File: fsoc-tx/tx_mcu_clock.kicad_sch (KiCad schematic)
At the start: 30 parts, among them J3 FTSH-105-01-L-DV-K, SW1 SW_RESET, SW2 USB_BOOT, U3 RP2354A, Y1 ABM8-272-T3, Y2 ASTX-H11-10.000MHz-T

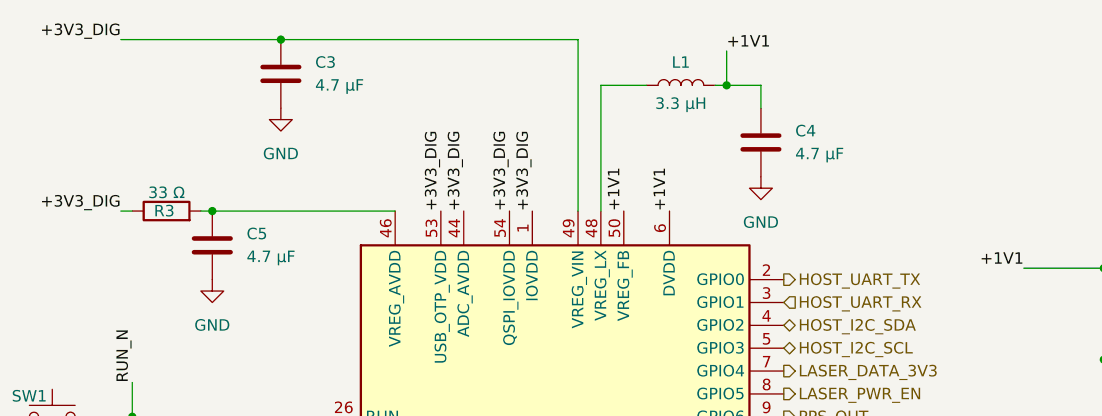
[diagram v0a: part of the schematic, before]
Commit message: ERC error excluded: TPS22919 QOD tied to VOUT intentionally
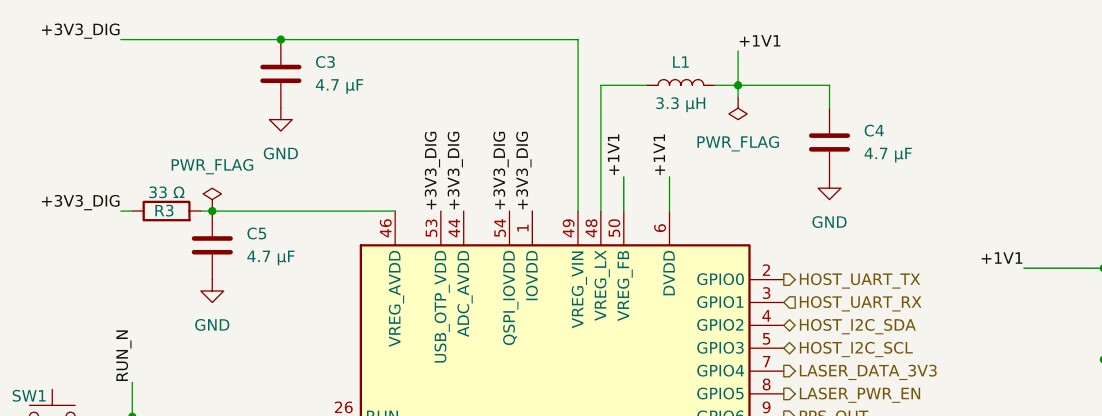
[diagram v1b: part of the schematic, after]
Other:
- moved on the sheet: C4
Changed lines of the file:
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@@
 	)
 	(junction
-		(at 179.07 29.21)
-		(diameter 0)
-		(color 0 0 0 0)
-	)
-	(junction
 		(at 199.39 148.59)
 		(diameter 0)
@@
 	)
 	(junction
+		(at 180.34 29.21)
+		(diameter 0)
+		(color 0 0 0 0)
+	)
+	(junction
 		(at 222.25 100.33)
 		(diameter 0)
@@
 	(wire
 		(pts
-			(xy 182.88 29.21) (xy 179.07 29.21)
+			(xy 190.5 29.21) (xy 180.34 29.21)
 		)
 		(stroke
@@
 	(wire
 		(pts
+			(xy 180.34 30.48) (xy 180.34 29.21)
+		)
+		(stroke
+			(width 0)
+			(type default)
+		)
+	)
+	(wire
+		(pts
 			(xy 111.76 148.59) (xy 118.11 148.59)
 		)
@@
 	(wire
 		(pts
-			(xy 179.07 25.4) (xy 179.07 29.21)
+			(xy 180.34 25.4) (xy 180.34 29.21)
 		)
 		(stroke
@@
 	(wire
 		(pts
-			(xy 177.8 29.21) (xy 179.07 29.21)
+			(xy 177.8 29.21) (xy 180.34 29.21)
 		)
 		(stroke
@@
 	(wire
 		(pts
+			(xy 167.64 39.37) (xy 167.64 43.18)
+		)
+		(stroke
+			(width 0)
+			(type default)
+		)
+	)
+	(wire
+		(pts
 			(xy 111.76 83.82) (xy 116.84 83.82)
 		)
@@
 	(wire
 		(pts
-			(xy 182.88 31.75) (xy 182.88 29.21)
+			(xy 190.5 31.75) (xy 190.5 29.21)
 		)
 		(stroke
@@
 	(wire
 		(pts
+			(xy 172.72 39.37) (xy 172.72 43.18)
+		)
+		(stroke
+			(width 0)
+			(type default)
+		)
+	)
+	(wire
+		(pts
 			(xy 130.81 77.47) (xy 130.81 76.2)
 		)
@@
 	)
 	(label "+1V1"
-		(at 167.64 43.18 90)
+		(at 167.64 39.37 90)
 		(effects
 			(font
@@
 	)
 	(label "+1V1"
-		(at 172.72 43.18 90)
+		(at 172.72 39.37 90)
 		(effects
 			(font
@@
 	)
 	(label "+1V1"
-		(at 179.07 25.4 0)
+		(at 180.34 25.4 0)
 		(effects
 			(font
@@
 	)
 	(symbol
+		(lib_id "power:PWR_FLAG")
+		(at 121.92 43.18 0)
+		(unit 1)
+		(body_style 1)
+		(exclude_from_sim no)
+		(in_bom yes)
+		(on_board yes)
+		(in_pos_files yes)
+		(dnp no)
+		(fields_autoplaced yes)
+		(property "Reference" "#FLG04"
+			(at 121.92 41.275 0)
+			(hide yes)
+			(show_name no)
+			(do_not_autoplace no)
+			(effects
+				(font
+					(size 1.27 1.27)
+				)
+			)
+		)
+		(property "Value" "PWR_FLAG"
+			(at 121.92 38.1 0)
+			(show_name no)
+			(do_not_autoplace no)
+			(effects
+				(font
+					(size 1.27 1.27)
+				)
+			)
+		)
+		(property "Footprint" ""
+			(at 121.92 43.18 0)
+			(hide yes)
+			(show_name no)
+			(do_not_autoplace no)
+			(effects
+				(font
+					(size 1.27 1.27)
+				)
+			)
+		)
+		(property "Datasheet" ""
+			(at 121.92 43.18 0)
+			(hide yes)
+			(show_name no)
+			(do_not_autoplace no)
+			(effects
+				(font
+					(size 1.27 1.27)
+				)
+			)
+		)
+		(property "Description" "Special symbol for telling ERC where power comes from"
+			(at 121.92 43.18 0)
+			(hide yes)
+			(show_name no)
+			(do_not_autoplace no)
+			(effects
+				(font
+					(size 1.27 1.27)
+				)
+			)
+		)
+		(pin "1"
+		)
+		(instances
+			(project "fsoc-tx"
+				(path "/d92cb11a-a3ee-43a3-bd30-881774176ced/1d4fb2f8-c912-4583-8b21-2ebadb633d8f"
+					(reference "#FLG04")
+					(unit 1)
+				)
+			)
+		)
+	)
+	(symbol
 		(lib_id "Switch:SW_Push")
 		(at 106.68 83.82 0)
@@
 	)
 	(symbol
+		(lib_id "power:PWR_FLAG")
+		(at 180.34 30.48 180)
+		(unit 1)
+		(body_style 1)
+		(exclude_from_sim no)
+		(in_bom yes)
+		(on_board yes)
+		(in_pos_files yes)
+		(dnp no)
+		(fields_autoplaced yes)
+		(property "Reference" "#FLG03"
+			(at 180.34 32.385 0)
+			(hide yes)
+			(show_name no)
+			(do_not_autoplace no)
+			(effects
+				(font
+					(size 1.27 1.27)
+				)
+			)
+		)
+		(property "Value" "PWR_FLAG"
+			(at 180.34 35.56 0)
+			(show_name no)
+			(do_not_autoplace no)
+			(effects
+				(font
+					(size 1.27 1.27)
+				)
+			)
+		)
+		(property "Footprint" ""
+			(at 180.34 30.48 0)
+			(hide yes)
+			(show_name no)
+			(do_not_autoplace no)
+			(effects
+				(font
+					(size 1.27 1.27)
+				)
+			)
+		)
+		(property "Datasheet" ""
+			(at 180.34 30.48 0)
+			(hide yes)
+			(show_name no)
+			(do_not_autoplace no)
+			(effects
+				(font
+					(size 1.27 1.27)
+				)
+			)
+		)
+		(property "Description" "Special symbol for telling ERC where power comes from"
+			(at 180.34 30.48 0)
+			(hide yes)
+			(show_name no)
+			(do_not_autoplace no)
+			(effects
+				(font
+					(size 1.27 1.27)
+				)
+			)
+		)
+		(pin "1"
+		)
+		(instances
+			(project "fsoc-tx"
+				(path "/d92cb11a-a3ee-43a3-bd30-881774176ced/1d4fb2f8-c912-4583-8b21-2ebadb633d8f"
+					(reference "#FLG03")
+					(unit 1)
+				)
+			)
+		)
+	)
+	(symbol
 		(lib_id "Device:R")
 		(at 116.84 43.18 90)
@@
 	(symbol
 		(lib_id "Device:C")
-		(at 182.88 35.56 0)
+		(at 190.5 35.56 0)
 		(unit 1)
 		(body_style 1)
@@
 		(fields_autoplaced yes)
 		(property "Reference" "C4"
-			(at 186.69 34.2899 0)
+			(at 194.31 34.2899 0)
 			(show_name no)
 			(do_not_autoplace no)
@@
 		)
 		(property "Value" "4.7 µF"
-			(at 186.69 36.8299 0)
+			(at 194.31 36.8299 0)
 			(show_name no)
 			(do_not_autoplace no)
@@
 		)
 		(property "Footprint" ""
-			(at 183.8452 39.37 0)
+			(at 191.4652 39.37 0)
 			(hide yes)
 			(show_name no)
@@
 		)
 		(property "Datasheet" ""
-			(at 182.88 35.56 0)
+			(at 190.5 35.56 0)
 			(hide yes)
 			(show_name no)
@@
 		)
 		(property "Description" "Unpolarized capacitor"
-			(at 182.88 35.56 0)
+			(at 190.5 35.56 0)
 			(hide yes)
 			(show_name no)
@@
 	(symbol
 		(lib_id "power:GND")
-		(at 182.88 39.37 0)
+		(at 190.5 39.37 0)
 		(unit 1)
 		(body_style 1)
@@
 		(fields_autoplaced yes)
 		(property "Reference" "#PWR011"
-			(at 182.88 45.72 0)
+			(at 190.5 45.72 0)
 			(hide yes)
 			(show_name no)
@@
 		)
 		(property "Value" "GND"
-			(at 182.88 44.45 0)
+			(at 190.5 44.45 0)
 			(show_name no)
 			(do_not_autoplace no)
@@
 		)
 		(property "Footprint" ""
-			(at 182.88 39.37 0)
+			(at 190.5 39.37 0)
 			(hide yes)
 			(show_name no)
@@
 		)
 		(property "Datasheet" ""
-			(at 182.88 39.37 0)
+			(at 190.5 39.37 0)
 			(hide yes)
 			(show_name no)
@@
 		)
 		(property "Description" "Power symbol creates a global label with name \"GND\" , ground"
-			(at 182.88 39.37 0)
+			(at 190.5 39.37 0)
 			(hide yes)
 			(show_name no)

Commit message: TX: fixing unassigned footprints
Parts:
- C10, C11, C12, C13, C14, C15, C16, C17, C18, C19, C20, C6, C8, C9: footprint (none) -> Capacitor_SMD:C_0603_1608Metric
- C3, C4, C5, C7: footprint (none) -> Capacitor_SMD:C_0805_2012Metric
- L1: footprint (none) -> fsoc_footprints:AOTA-B201610S3R3-101-T
- R3, R4, R5, R6, R7: footprint (none) -> Resistor_SMD:R_0603_1608Metric
- SW1, SW2: footprint (none) -> Button_Switch_SMD:SW_SPST_PTS645Sx43SMTR92
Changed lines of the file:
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@@
 			)
 		)
-		(property "Footprint" ""
+		(property "Footprint" "Capacitor_SMD:C_0603_1608Metric"
 			(at 162.8648 148.59 0)
 			(hide yes)
@@
 			)
 		)
-		(property "Footprint" ""
+		(property "Footprint" "Capacitor_SMD:C_0603_1608Metric"
 			(at 220.98 70.8152 0)
 			(hide yes)
@@
 			)
 		)
-		(property "Footprint" ""
+		(property "Footprint" "fsoc_footprints:AOTA-B201610S3R3-101-T"
 			(at 173.99 29.21 0)
 			(hide yes)
@@
 			)
 		)
-		(property "Footprint" ""
+		(property "Footprint" "Capacitor_SMD:C_0603_1608Metric"
 			(at 151.4348 148.59 0)
 			(hide yes)
@@
 			)
 		)
-		(property "Footprint" ""
+		(property "Footprint" "Capacitor_SMD:C_0603_1608Metric"
 			(at 175.5648 148.59 0)
 			(hide yes)
@@
 			)
 		)
-		(property "Footprint" ""
+		(property "Footprint" "Capacitor_SMD:C_0603_1608Metric"
 			(at 223.2152 109.22 0)
 			(hide yes)
@@
 			)
 		)
-		(property "Footprint" ""
+		(property "Footprint" "Capacitor_SMD:C_0603_1608Metric"
 			(at 113.9952 121.92 0)
 			(hide yes)
@@
 			)
 		)
-		(property "Footprint" ""
+		(property "Footprint" "Capacitor_SMD:C_0603_1608Metric"
 			(at 113.9952 104.14 0)
 			(hide yes)
@@
 			)
 		)
-		(property "Footprint" ""
+		(property "Footprint" "Capacitor_SMD:C_0805_2012Metric"
 			(at 228.6 58.7248 0)
 			(hide yes)
@@
 			)
 		)
-		(property "Footprint" ""
+		(property "Footprint" "Capacitor_SMD:C_0603_1608Metric"
 			(at 209.8548 148.59 0)
 			(hide yes)
@@
 			)
 		)
-		(property "Footprint" ""
+		(property "Footprint" "Capacitor_SMD:C_0603_1608Metric"
 			(at 117.1448 148.59 0)
 			(hide yes)
@@
 			)
 		)
-		(property "Footprint" ""
+		(property "Footprint" "Capacitor_SMD:C_0603_1608Metric"
 			(at 186.9948 148.59 0)
 			(hide yes)
@@
 			)
 		)
-		(property "Footprint" ""
+		(property "Footprint" "Capacitor_SMD:C_0805_2012Metric"
 			(at 122.8852 50.8 0)
 			(hide yes)
@@
 			)
 		)
-		(property "Footprint" ""
+		(property "Footprint" "Capacitor_SMD:C_0603_1608Metric"
 			(at 128.5748 148.59 0)
 			(hide yes)
@@
 			)
 		)
-		(property "Footprint" ""
+		(property "Footprint" "Button_Switch_SMD:SW_SPST_PTS645Sx43SMTR92"
 			(at 106.68 78.74 0)
 			(hide yes)
@@
 			)
 		)
-		(property "Footprint" ""
+		(property "Footprint" "Resistor_SMD:R_0603_1608Metric"
 			(at 116.84 44.958 90)
 			(hide yes)
@@
 			)
 		)
-		(property "Footprint" ""
+		(property "Footprint" "Capacitor_SMD:C_0603_1608Metric"
 			(at 198.4248 148.59 0)
 			(hide yes)
@@
 			)
 		)
-		(property "Footprint" ""
+		(property "Footprint" "Resistor_SMD:R_0603_1608Metric"
 			(at 120.65 85.598 90)
 			(hide yes)
@@
 			)
 		)
-		(property "Footprint" ""
+		(property "Footprint" "Resistor_SMD:R_0603_1608Metric"
 			(at 128.27 112.522 90)
 			(hide yes)
@@
 			)
 		)
-		(property "Footprint" ""
+		(property "Footprint" "Capacitor_SMD:C_0603_1608Metric"
 			(at 140.0048 148.59 0)
 			(hide yes)
@@
 			)
 		)
-		(property "Footprint" ""
+		(property "Footprint" "Capacitor_SMD:C_0805_2012Metric"
 			(at 130.5052 31.75 0)
 			(hide yes)
@@
 			)
 		)
-		(property "Footprint" ""
+		(property "Footprint" "Capacitor_SMD:C_0603_1608Metric"
 			(at 228.6 48.5648 0)
 			(hide yes)
@@
 			)
 		)
-		(property "Footprint" ""
+		(property "Footprint" "Resistor_SMD:R_0603_1608Metric"
 			(at 124.46 70.612 90)
 			(hide yes)
@@
 			)
 		)
-		(property "Footprint" ""
+		(property "Footprint" "Resistor_SMD:R_0603_1608Metric"
 			(at 124.46 75.692 90)
 			(hide yes)
@@
 			)
 		)
-		(property "Footprint" ""
+		(property "Footprint" "Capacitor_SMD:C_0805_2012Metric"
 			(at 191.4652 39.37 0)
 			(hide yes)
@@
 			)
 		)
-		(property "Footprint" ""
+		(property "Footprint" "Button_Switch_SMD:SW_SPST_PTS645Sx43SMTR92"
 			(at 104.14 60.96 0)
 			(hide yes)

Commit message: TX PCB: DONE
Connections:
- net USB_DM renamed USB_DN
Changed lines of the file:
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@@
 		)
 	)
-	(hierarchical_label "USB_DM"
+	(hierarchical_label "USB_DN"
 		(shape bidirectional)
 		(at 118.11 72.39 180)

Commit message: TX PCB: U3 footprint changed to the thermal vias version
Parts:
- U3: footprint Package_DFN_QFN:QFN-60-1EP_7x7mm_P0.4mm_EP3.4x3.4mm -> Package_DFN_QFN:QFN-60-1EP_7x7mm_P0.4mm_EP3.4x3.4mm_ThermalVias
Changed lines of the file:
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@@
 			)
 		)
-		(property "Footprint" "Package_DFN_QFN:QFN-60-1EP_7x7mm_P0.4mm_EP3.4x3.4mm"
+		(property "Footprint" "Package_DFN_QFN:QFN-60-1EP_7x7mm_P0.4mm_EP3.4x3.4mm_ThermalVias"
 			(at 160.02 88.9 0)
 			(hide yes)

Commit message: Switching ASTX-H11 to SiT5346 and SiT5346 datasheet
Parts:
- removed Y2: ASTX-H11-10.000MHz-T, fsoc_footprints:ASTX-H11_3225, symbol fsoc_symbols:ASTX-H11
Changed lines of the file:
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@@
-	)
-	(junction
-		(at 222.25 100.33)
-		(diameter 0)
-		(color 0 0 0 0)
 	)
 	(junction
@@
 	(wire
 		(pts
-			(xy 222.25 100.33) (xy 222.25 101.6)
-		)
-		(stroke
-			(width 0)
-			(type default)
-		)
-	)
-	(wire
-		(pts
 			(xy 163.83 138.43) (xy 163.83 139.7)
 		)
@@
 	(wire
 		(pts
-			(xy 222.25 95.25) (xy 222.25 100.33)
+			(xy 222.25 95.25) (xy 222.25 101.6)
 		)
 		(stroke
@@
 					(unit 1)
 				)
-			)
-		)
-	)
-	(symbol
-		(lib_id "fsoc_symbols:ASTX-H11")
-		(at 229.87 100.33 0)
-		(unit 1)
-		(body_style 1)
-		(exclude_from_sim no)
-		(in_bom yes)
-		(on_board yes)
-		(in_pos_files yes)
-		(dnp no)
-		(property "Reference" "Y2"
-			(at 234.188 103.124 0)
-			(hide yes)
-			(show_name no)
-			(do_not_autoplace no)
-			(effects
-				(font
-					(size 1.27 1.27)
-				)
-			)
-		)
-		(property "Value" "ASTX-H11-10.000MHz-T"
-			(at 235.712 103.632 0)
-			(show_name no)
-			(do_not_autoplace no)
-			(effects
-				(font
-					(size 0.508 0.508)
-				)
-			)
-		)
-		(property "Footprint" "fsoc_footprints:ASTX-H11_3225"
-			(at 229.87 115.57 0)
-			(hide yes)
-			(show_name no)
-			(do_not_autoplace no)
-			(effects
-				(font
-					(size 1.27 1.27)
-				)
-			)
-		)
-		(property "Datasheet" "https://abracon.com/Oscillators/ASTX-H11.pdf"
-			(at 231.902 120.396 0)
-			(hide yes)
-			(show_name no)
-			(do_not_autoplace no)
-			(effects
-				(font
-					(size 1.27 1.27)
-				)
-			)
-		)
-		(property "Description" "10 MHz HCMOS TCXO, 3.3 V nominal, 3.2 x 2.5 x 1.0 mm, 4-SMD"
-			(at 229.87 118.11 0)
-			(hide yes)
-			(show_name no)
-			(do_not_autoplace no)
-			(effects
-				(font
-					(size 1.27 1.27)
-				)
-			)
-		)
-		(property "Manufacturer" "Abracon"
-			(at 229.616 123.19 0)
-			(hide yes)
-			(show_name no)
-			(do_not_autoplace no)
-			(effects
-				(font
-					(size 1.27 1.27)
-				)
-			)
-		)
-		(property "MPN" "ASTX-H11-10.000MHz-T"
-			(at 229.87 126.238 0)
-			(hide yes)
-			(show_name no)
-			(do_not_autoplace no)
-			(effects
-				(font
-					(size 1.27 1.27)
-				)
-			)
-		)
-		(pin "4"
-		)
-		(pin "1"
-		)
-		(pin "3"
-		)
-		(pin "2"
-		)
-		(instances
-			(project "fsoc-tx"
-				(path "/d92cb11a-a3ee-43a3-bd30-881774176ced/1d4fb2f8-c912-4583-8b21-2ebadb633d8f"
-					(reference "Y2")
-					(unit 1)
-				)

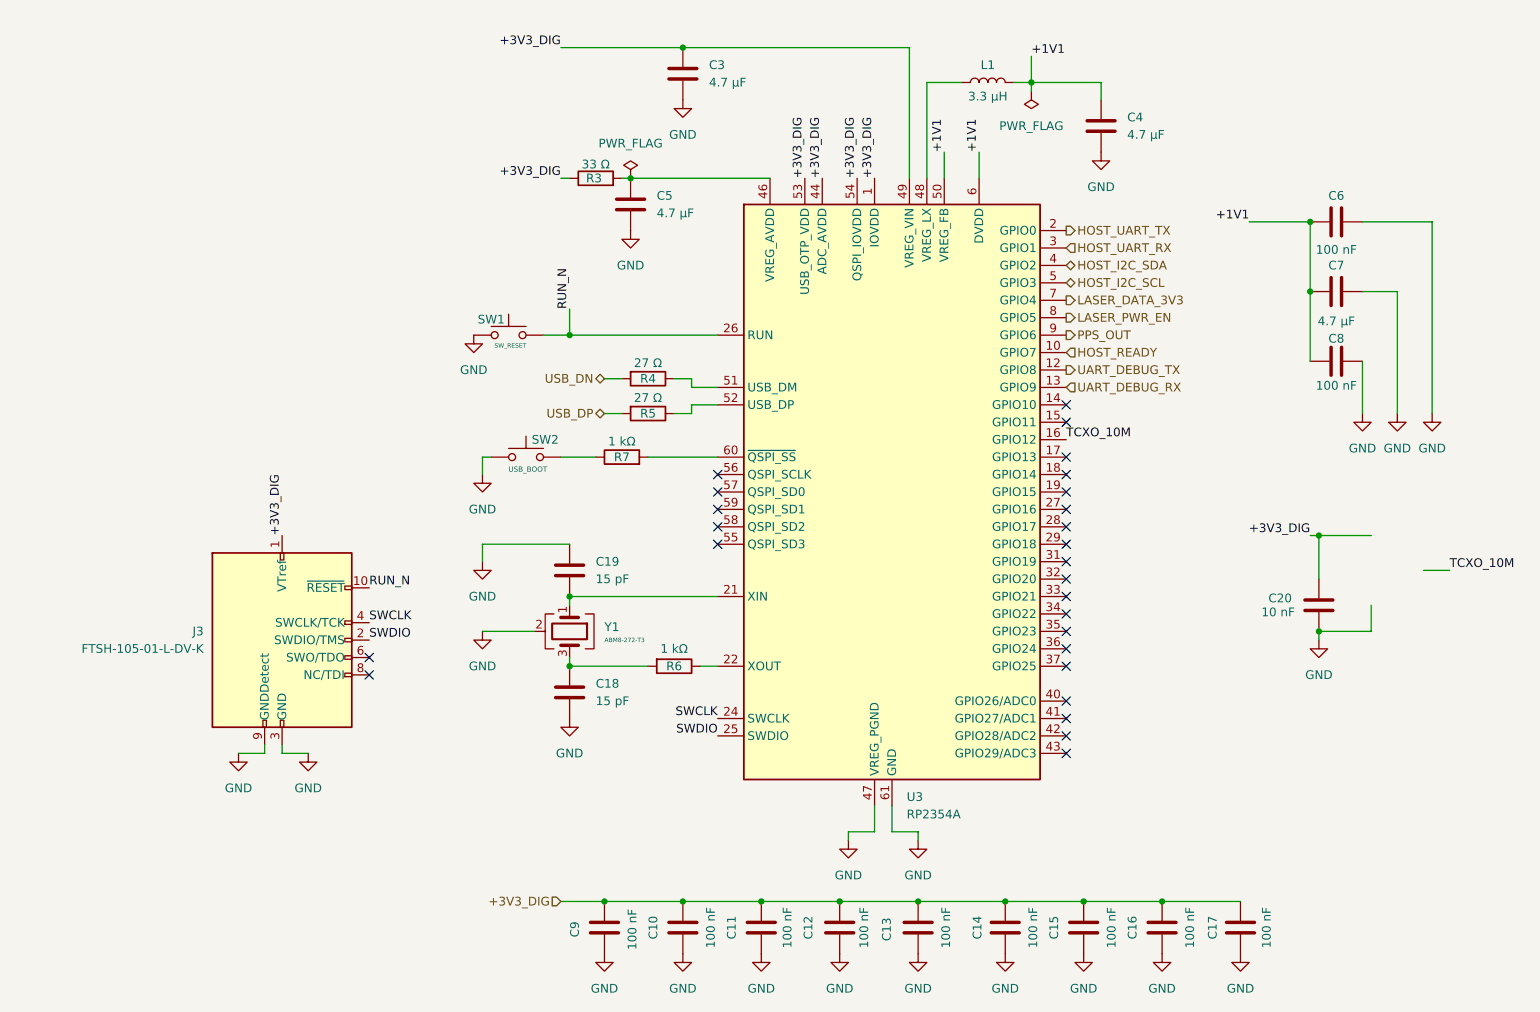
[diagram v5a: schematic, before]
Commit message: Switching ASTX-H11 to SiT5346 and SiT5346 datasheet
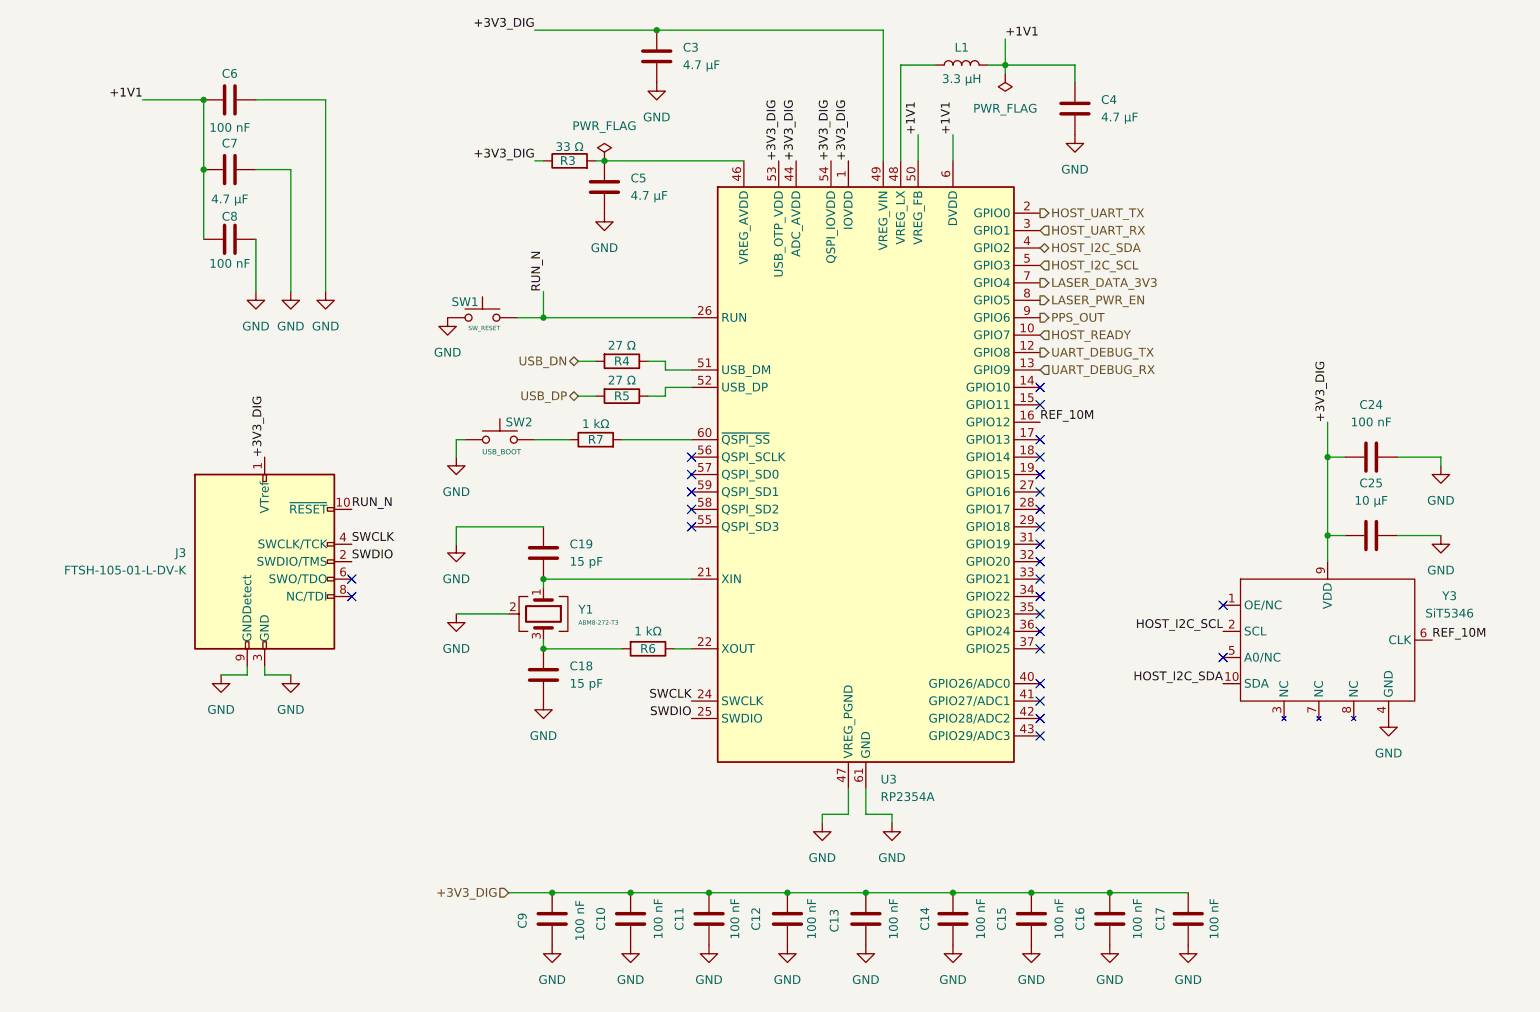
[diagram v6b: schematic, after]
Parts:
- removed C20: 10 nF, Capacitor_SMD:C_0603_1608Metric, symbol Device:C
- added C24: 100 nF, Capacitor_SMD:C_0603_1608Metric, symbol Device:C
- added C25: 10 µF, Capacitor_SMD:C_0805_2012Metric, symbol Device:C
- added Y3: SiT5346, fsoc_footprints:SiT5346_5.0x3.2mm_10L, symbol fsoc_symbols:SiT5346_DCTCXO
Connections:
- net +3V3_DIG: now also C24.1, C25.1, Y3.9 (VDD)
- net GND: now also C24.2, C25.2, Y3.4 (GND)
- net HOST_I2C_SCL: now also Y3.2 (SCL)
- net HOST_I2C_SDA: now also Y3.10 (SDA)
- net TCXO_10M renamed REF_10M
- net REF_10M: now also Y3.6 (CLK)
- no-connect marks 26 -> 28
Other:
- moved on the sheet: C10, C11, C12, C13, C14, C15, C16, C17, C18, C19, C3, C4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
